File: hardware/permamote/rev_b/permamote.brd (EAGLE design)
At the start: 27 x 60 mm, 131 parts, among them J1 TC2030-JLINK-NL, J5 MICRO_USB_B_HIROSE_ZX62R-B-5P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, Q1 PMDXB950UPEL, Q10 PMDXB950UPEL, Q2 PMDXB950UPEL, Q3 PMDXB950UPEL, Q4 PMDXB950UPEL, Q5 PMDXB950UPEL, Q6 PMDXB950UPEL, Q7 PMDXB950UPEL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

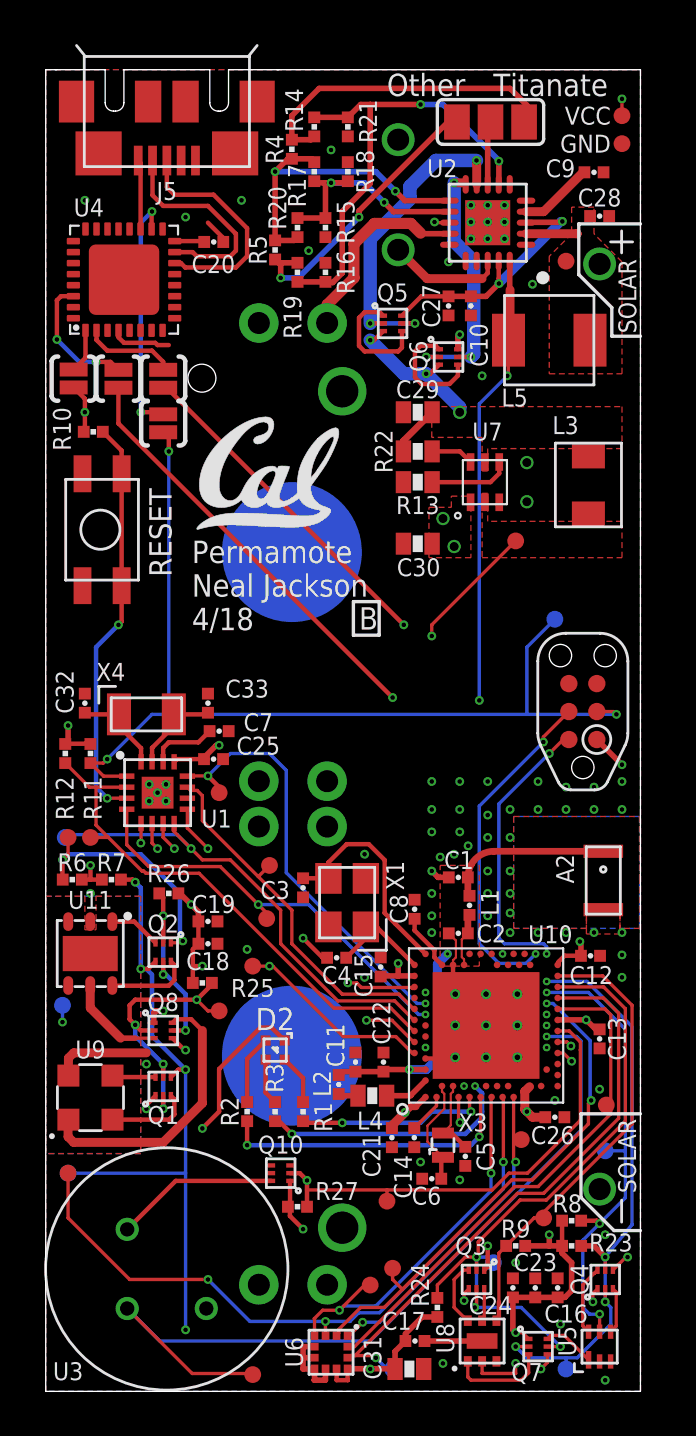
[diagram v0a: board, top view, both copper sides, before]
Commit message: Move coin cell holder out from under PIR
Move button/led to debug edge of board
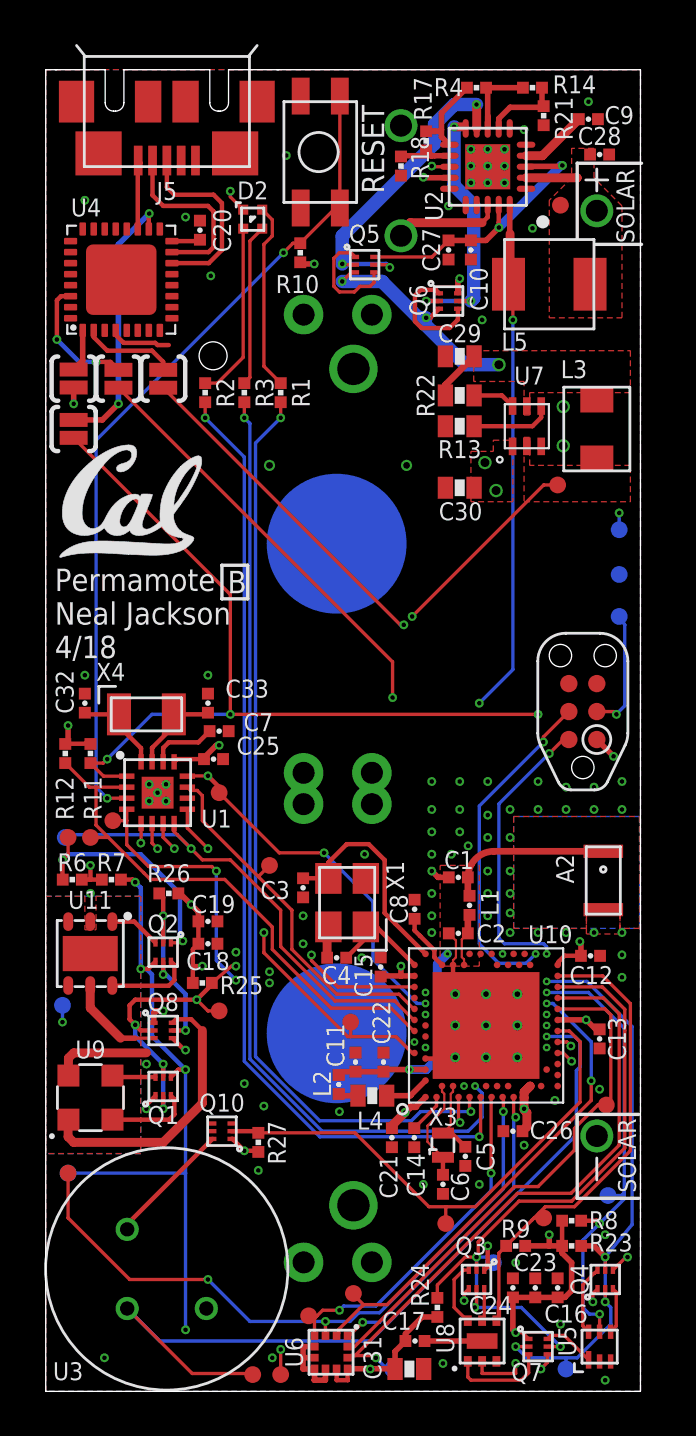
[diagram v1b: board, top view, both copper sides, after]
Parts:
- removed R15, R16, R19, R20, R5: DNP, passives:0402_RES
- removed SJ1: (no value), jumper:SJ_2
- moved D2 37.7 mm to (9.40, 53.2), turned to 90 degrees
- moved R2 32.7 mm to (7.24, 45.3)
- moved R3 32.7 mm to (9.02, 45.3)
- moved R1 32.7 mm to (10.7, 45.3)
- moved S1 19.8 mm to (12.4, 56.3)
- moved TP27 19.6 mm to (26.0, 37.1), flipped to the bottom
- moved TP26 18.8 mm to (26.0, 39.1), flipped to the bottom
- moved TP3 15.3 mm to (10.7, 0.76), turned to 180 degrees
- moved R10 12.4 mm to (11.6, 51.7), turned to 270 degrees
- moved R14 10.1 mm to (22.1, 59.2), turned to 180 degrees
- moved R21 8.90 mm to (22.6, 57.9)
- moved R4 8.84 mm to (19.6, 59.2), turned to 0 degrees
- moved TP14 8.28 mm to (3.05, 25.9)
- moved U$2 6.35 mm to (0.64, 37.8)
- moved R17 5.27 mm to (17.3, 56.8)
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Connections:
- removed net N$1: R14.2, R4.2, SJ1.3
- removed net N$16: R19.2, R5.2, SJ1.1
- net GND: no longer R15.1, R16.1
- net N$18: no longer R16.2, R19.1
- net N$32: now also R14.2, R4.2; no longer SJ1.2
- net N$57: no longer R15.2, R20.1
- net N$58: no longer R20.2, R5.1
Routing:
- net LED_RED: track 8.55 -> 42.0 mm
- net LED_BLUE: track 11.5 -> 43.6 mm
- net LED_GREEN: track 13.6 -> 44.6 mm
- net !RTC_EXTR: track 18.7 -> 38.0 mm
- net N$18: track 21.2 -> 3.60 mm, vias 2 -> 0
- net N$16: track 12.9 -> 0.00 mm, vias 2 -> 0
- net N$58: track 14.8 -> 4.39 mm, vias 2 -> 0
- net N$1: track 14.5 -> 6.22 mm, vias 0 -> 2
- net N$57: track 10.4 -> 2.55 mm, vias 2 -> 0
- net VSOL: track 41.8 -> 48.5 mm
- net N$15: track 2.28 -> 8.54 mm
- net N$19: track 2.11 -> 7.35 mm
- net N$17: track 3.14 -> 8.05 mm
- net SW: track 30.1 -> 33.9 mm
- net VSW: track 9.39 -> 12.9 mm
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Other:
- board text added: "CR123A PACK +"
- board text added: "CR123A PACK -"
- board text removed: "CR123A PACK"
- board text removed: "Other"
- board text removed: "Titanate"

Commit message: move led even closer to edge
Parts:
- moved D2 8.08 mm to (15.1, 58.9)
- moved R1 6.81 mm to (12.3, 51.9)
- moved R2 6.81 mm to (8.89, 51.9)
- moved R3 6.78 mm to (10.5, 51.9)
- moved R10 3.51 mm to (8.89, 54.0)
- moved R18 0.63 mm to (16.1, 55.0)
- moved BT1 0.28 mm to (16.0, 54.7)
- moved Q5 0.28 mm to (14.2, 51.0)
- moved R17 0.25 mm to (17.5, 56.8)
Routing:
- net LED_RED: track 42.0 -> 50.0 mm
- net LED_BLUE: track 43.6 -> 50.7 mm
- net LED_GREEN: track 44.6 -> 50.5 mm
- net !RTC_EXTR: track 38.0 -> 42.5 mm, vias 2 -> 4
- net N$15: track 8.54 -> 10.8 mm
- net N$19: track 7.35 -> 8.60 mm
- net N$17: track 8.05 -> 8.82 mm
- net N$58: track 4.39 -> 3.68 mm
- net VOC_SAMP_VSTOR: track 13.7 -> 14.2 mm
- net GND: vias 100 -> 105

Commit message: align light sensors
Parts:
- moved U8 0.13 mm to (19.8, 2.16)
- moved U5 0.13 mm to (25.1, 2.16)
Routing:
- net GND: track 31.0 -> 27.7 mm
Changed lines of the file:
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@@
 </polygon>
 <polygon width="0.1016" layer="41">
-<vertex x="20.066" y="1.651"/>
-<vertex x="20.066" y="1.143"/>
-<vertex x="20.193" y="1.143"/>
-<vertex x="20.193" y="1.651"/>
+<vertex x="20.066" y="1.524"/>
+<vertex x="20.066" y="1.016"/>
+<vertex x="20.193" y="1.016"/>
+<vertex x="20.193" y="1.524"/>
 </polygon>
 <text x="8.255" y="36.233" size="1.016" layer="25" font="vector" ratio="12">&gt;REV</text>
@@
 <attribute name="NAME" x="23.114" y="5.842" size="0.8128" layer="26" font="vector" ratio="12" rot="MR90"/>
 </element>
-<element name="U5" library="chips" package="ODFN-6-1.5MMX1.6MM" value="ISL29125" x="25.146" y="2.032" smashed="yes" rot="R90">
-<attribute name="DIGIKEY" value="ISL29125IROZ-T7ACT-ND " x="25.146" y="2.032" size="1.778" layer="27" rot="R90" display="off"/>
-<attribute name="MANUFACTURER" value="INTERSIL" x="25.146" y="2.032" size="1.778" layer="27" rot="R90" display="off"/>
-<attribute name="MPN" value="ISL29125IROZ-T7A" x="25.146" y="2.032" size="1.778" layer="27" rot="R90" display="off"/>
-<attribute name="NAME" x="23.268" y="2.282" size="0.8128" layer="25" font="vector" ratio="12" rot="R90" align="top-center"/>
-</element>
-<element name="U8" library="chips" package="UDFN-6-EXPOSED" value="MAX44009" x="19.812" y="2.286" smashed="yes" rot="R90">
-<attribute name="DIGIKEY" value="MAX44009EDT+TCT-ND" x="19.812" y="2.286" size="1.778" layer="27" rot="R90" display="off"/>
-<attribute name="MANUFACTURER" value="MAXIM" x="19.812" y="2.286" size="1.778" layer="27" rot="R90" display="off"/>
-<attribute name="MPN" value="MAX44009EDT+T" x="19.812" y="2.286" size="1.778" layer="27" rot="R90" display="off"/>
-<attribute name="NAME" x="18.542" y="2.413" size="0.8128" layer="25" font="vector" ratio="12" rot="R90" align="bottom-center"/>
+<element name="U5" library="chips" package="ODFN-6-1.5MMX1.6MM" value="ISL29125" x="25.146" y="2.159" smashed="yes" rot="R90">
+<attribute name="DIGIKEY" value="ISL29125IROZ-T7ACT-ND " x="25.146" y="2.159" size="1.778" layer="27" rot="R90" display="off"/>
+<attribute name="MANUFACTURER" value="INTERSIL" x="25.146" y="2.159" size="1.778" layer="27" rot="R90" display="off"/>
+<attribute name="MPN" value="ISL29125IROZ-T7A" x="25.146" y="2.159" size="1.778" layer="27" rot="R90" display="off"/>
+<attribute name="NAME" x="23.268" y="2.409" size="0.8128" layer="25" font="vector" ratio="12" rot="R90" align="top-center"/>
+</element>
+<element name="U8" library="chips" package="UDFN-6-EXPOSED" value="MAX44009" x="19.812" y="2.159" smashed="yes" rot="R90">
+<attribute name="DIGIKEY" value="MAX44009EDT+TCT-ND" x="19.812" y="2.159" size="1.778" layer="27" rot="R90" display="off"/>
+<attribute name="MANUFACTURER" value="MAXIM" x="19.812" y="2.159" size="1.778" layer="27" rot="R90" display="off"/>
+<attribute name="MPN" value="MAX44009EDT+T" x="19.812" y="2.159" size="1.778" layer="27" rot="R90" display="off"/>
+<attribute name="NAME" x="18.542" y="2.286" size="0.8128" layer="25" font="vector" ratio="12" rot="R90" align="bottom-center"/>
 </element>
 <element name="C23" library="passives" package="0402_CAP" value="1uF" x="22.225" y="4.699" smashed="yes" rot="R90">
@@
 <wire x1="5.0749" y1="47.498" x2="5.588" y2="47.498" width="0.2032" layer="1"/>
 <via x="8.636" y="19.939" extent="1-16" drill="0.2032"/>
-<wire x1="19.812" y1="1.361" x2="19.812" y2="0.8128" width="0.1524" layer="1"/>
-<wire x1="21.336" y1="0.8128" x2="19.812" y2="0.8128" width="0.1524" layer="1"/>
-<wire x1="21.336" y1="0.8128" x2="21.336" y2="1.27" width="0.1524" layer="1"/>
 <via x="21.336" y="1.27" extent="1-16" drill="0.2032"/>
 <via x="21.336" y="5.842" extent="1-16" drill="0.2032"/>
@@
 <wire x1="17.526" y1="23.622" x2="17.815" y2="23.333" width="0.254" layer="1"/>
 <wire x1="17.815" y1="23.333" x2="18.29893125" y2="23.333" width="0.254" layer="1"/>
-<wire x1="19.812" y1="2.286" x2="17.19706875" y2="2.286" width="0.254" layer="1"/>
 <via x="18.034" y="1.27" extent="1-16" drill="0.2032"/>
 <via x="25.4" y="7.112" extent="1-16" drill="0.2032"/>
@@
 <via x="12.954" y="33.242" extent="1-16" drill="0.2032"/>
 <via x="7.747" y="39.084" extent="1-16" drill="0.2032"/>
+<wire x1="19.812" y1="1.234" x2="19.812" y2="0.6858" width="0.254" layer="1"/>
+<wire x1="19.812" y1="0.6858" x2="21.082" y2="0.6858" width="0.254" layer="1"/>
 </signal>
 <signal name="N$8">
@@
 <via x="22.742" y="18.11" extent="1-16" drill="0.1524"/>
 <via x="25.146" y="3.5052" extent="1-16" drill="0.2032"/>
-<wire x1="25.146" y1="2.707" x2="25.146" y2="3.5052" width="0.1524" layer="1"/>
+<wire x1="25.146" y1="2.834" x2="25.146" y2="3.5052" width="0.1524" layer="1"/>
 <wire x1="25.146" y1="3.5052" x2="24.6888" y2="3.5052" width="0.1524" layer="16"/>
 <wire x1="24.6888" y1="3.5052" x2="24.384" y2="3.81" width="0.1524" layer="16"/>
@@
 <contactref element="U8" pad="4"/>
 <contactref element="R9" pad="1"/>
-<wire x1="20.462" y1="3.211" x2="20.574" y2="3.323" width="0.2032" layer="1"/>
-<wire x1="20.574" y1="3.323" x2="20.574" y2="4.064" width="0.2032" layer="1"/>
-<wire x1="20.574" y1="4.064" x2="20.574" y2="6.27506875" width="0.1524" layer="1"/>
-<wire x1="20.574" y1="6.27506875" x2="20.90293125" y2="6.604" width="0.1524" layer="1"/>
+<wire x1="20.90293125" y1="6.604" x2="20.574" y2="6.27506875" width="0.1524" layer="1"/>
 <wire x1="20.90293125" y1="6.604" x2="20.828" y2="6.67893125" width="0.2032" layer="1"/>
 <contactref element="U10" pad="AD22"/>
 <wire x1="23.242" y1="18.86" x2="25.285" y2="18.86" width="0.1524" layer="1"/>
 <contactref element="TP21" pad="P$1"/>
-<wire x1="20.90293125" y1="6.604" x2="22.071965625" y2="7.773034375" width="0.1524" layer="1"/>
-<wire x1="22.071965625" y1="7.773034375" x2="22.17293125" y2="7.874" width="0.1524" layer="1"/>
+<wire x1="20.90293125" y1="6.604" x2="22.17293125" y2="7.874" width="0.1524" layer="1"/>
 <wire x1="22.17293125" y1="7.874" x2="22.606" y2="7.874" width="0.1524" layer="1"/>
 <wire x1="22.606" y1="8.1294875" x2="22.606" y2="7.874" width="0.1524" layer="1"/>
@@
 <wire x1="22.68093125" y1="8.382" x2="22.17293125" y2="7.874" width="0.1524" layer="1"/>
 <wire x1="26.543" y1="17.602" x2="26.543" y2="10.922" width="0.1524" layer="1"/>
+<wire x1="20.574" y1="3.196" x2="20.462" y2="3.084" width="0.1524" layer="1"/>
+<wire x1="20.574" y1="6.27506875" x2="20.574" y2="3.196" width="0.1524" layer="1"/>
 </signal>
 <signal name="N$25">
@@
 <contactref element="Q7" pad="6"/>
 <wire x1="22.777" y1="2.382" x2="22.935" y2="2.54" width="0.1524" layer="1"/>
-<wire x1="23.538" y1="2.54" x2="24.646" y2="1.432" width="0.1524" layer="1"/>
-<wire x1="22.935" y1="2.54" x2="23.538" y2="2.54" width="0.1524" layer="1"/>
+<wire x1="23.665" y1="2.54" x2="24.646" y2="1.559" width="0.1524" layer="1"/>
+<wire x1="22.935" y1="2.54" x2="23.665" y2="2.54" width="0.1524" layer="1"/>
 </signal>
 <signal name="N$20">
 <contactref element="U8" pad="1"/>
 <contactref element="Q7" pad="3"/>
-<wire x1="19.162" y1="1.361" x2="19.162" y2="0.65" width="0.1524" layer="1"/>
-<wire x1="19.162" y1="0.65" x2="19.304" y2="0.508" width="0.1524" layer="1"/>
-<wire x1="19.304" y1="0.508" x2="21.59" y2="0.508" width="0.1524" layer="1"/>
+<wire x1="19.162" y1="1.234" x2="19.162" y2="0.523" width="0.1524" layer="1"/>
+<wire x1="19.162" y1="0.523" x2="19.304" y2="0.381" width="0.1524" layer="1"/>
+<wire x1="19.304" y1="0.381" x2="21.463" y2="0.381" width="0.1524" layer="1"/>
 <wire x1="21.927" y1="0.845" x2="21.927" y2="1.682" width="0.1524" layer="1"/>
-<wire x1="21.59" y1="0.508" x2="21.927" y2="0.845" width="0.1524" layer="1"/>
+<wire x1="21.463" y1="0.381" x2="21.927" y2="0.845" width="0.1524" layer="1"/>
 </signal>
 <signal name="N$44">
@@
 <contactref element="Q3" pad="3"/>
 <contactref element="U8" pad="6"/>
-<wire x1="19.162" y1="3.211" x2="19.141" y2="3.211" width="0.1524" layer="1"/>
+<wire x1="19.162" y1="3.084" x2="19.141" y2="3.211" width="0.1524" layer="1"/>
 <wire x1="19.141" y1="3.211" x2="18.542" y2="3.81" width="0.1524" layer="1"/>
 <wire x1="18.542" y1="5.08" x2="18.542" y2="3.81" width="0.1524" layer="1"/>
@@
 <contactref element="U8" pad="5"/>
 <wire x1="19.908" y1="4.655" x2="19.908" y2="3.307" width="0.1524" layer="1"/>
-<wire x1="19.908" y1="3.307" x2="19.812" y2="3.211" width="0.1524" layer="1"/>
+<wire x1="19.908" y1="3.307" x2="19.812" y2="3.084" width="0.1524" layer="1"/>
 </signal>
 <signal name="N$54">
 <contactref element="Q4" pad="3"/>
 <contactref element="U5" pad="4"/>
-<wire x1="25.75" y1="4.655" x2="25.9" y2="4.505" width="0.1524" layer="1"/>
-<wire x1="25.9" y1="4.505" x2="25.9" y2="2.961" width="0.1524" layer="1"/>
-<wire x1="25.9" y1="2.961" x2="25.646" y2="2.707" width="0.1524" layer="1"/>
+<wire x1="25.9" y1="4.505" x2="25.75" y2="4.655" width="0.1524" layer="1"/>
+<wire x1="25.646" y1="2.834" x2="25.9" y2="3.088" width="0.1524" layer="1"/>
+<wire x1="25.9" y1="3.088" x2="25.9" y2="4.505" width="0.1524" layer="1"/>
 </signal>
 <signal name="N$55">
@@
 <wire x1="24.902" y1="5.357" x2="24.89739375" y2="5.357" width="0.1524" layer="1"/>
 <wire x1="24.384" y1="4.84360625" x2="24.89739375" y2="5.357" width="0.1524" layer="1"/>
-<wire x1="24.646" y1="2.707" x2="24.384" y2="2.969" width="0.1524" layer="1"/>
-<wire x1="24.384" y1="2.969" x2="24.384" y2="4.84360625" width="0.1524" layer="1"/>
+<wire x1="24.646" y1="2.834" x2="24.384" y2="3.096" width="0.1524" layer="1"/>
+<wire x1="24.384" y1="3.096" x2="24.384" y2="4.84360625" width="0.1524" layer="1"/>
 </signal>
 <signal name="LBST">
